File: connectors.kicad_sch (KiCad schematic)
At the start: 2 parts, among them J1 CM4_Plug_Module_Hirose_DF40_2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

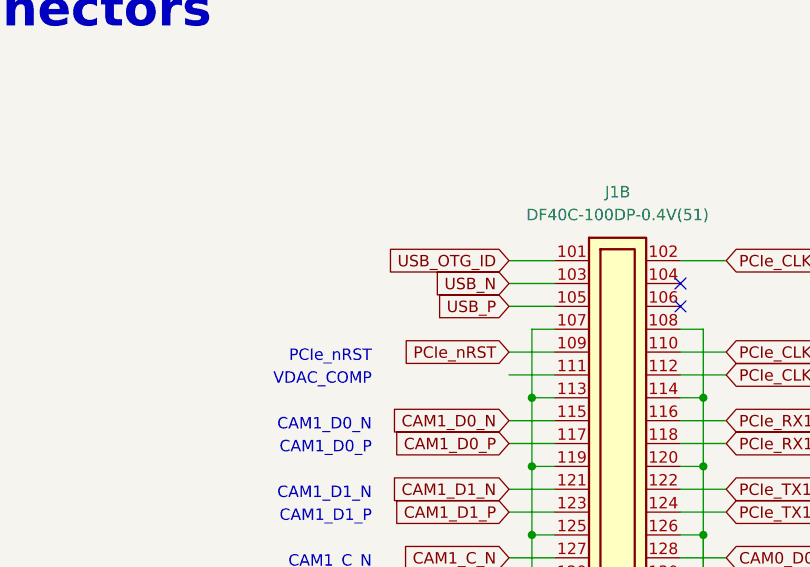
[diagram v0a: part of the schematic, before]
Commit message: [#54828] Add USB hub, change LBEE5PK2AE connection to USB
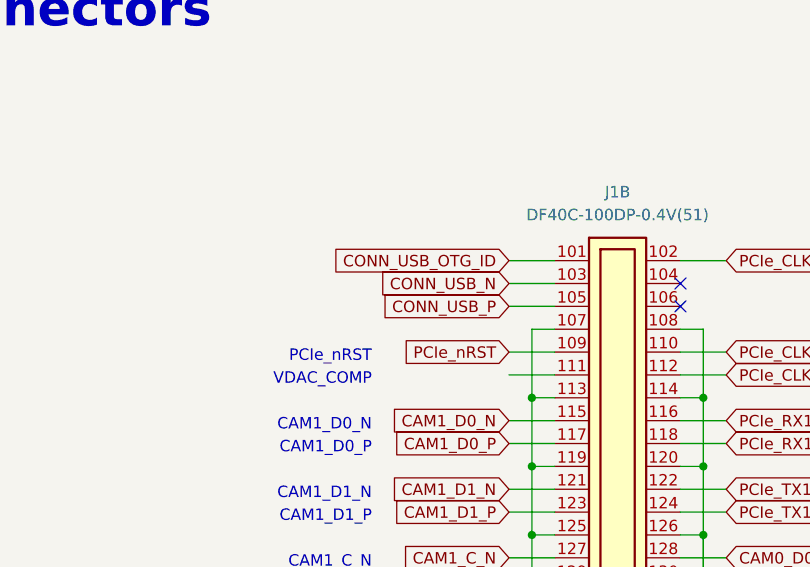
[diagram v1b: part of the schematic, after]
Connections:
- net USB_N renamed CONN_USB_N
- net USB_OTG_ID renamed CONN_USB_OTG_ID
- net USB_P renamed CONN_USB_P
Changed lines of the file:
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@@
+    )
+  )
+  (global_label "CONN_USB_OTG_ID" (shape input) (at 283.21 78.74 180) (fields_autoplaced)
+    (effects (font (size 1.27 1.27)) (justify right))
+    (property "Intersheetrefs" "${INTERSHEET_REFS}" (at 262.8076 78.74 0)
+      (effects (font (size 1.27 1.27)) (justify right) hide)
     )
   )
@@
     )
   )
-  (global_label "USB_N" (shape input) (at 283.21 81.28 180) (fields_autoplaced)
-    (effects (font (size 1.27 1.27)) (justify right))
-    (property "Intersheetrefs" "${INTERSHEET_REFS}" (at 274.6888 81.2006 0)
+  (global_label "CONN_USB_N" (shape input) (at 283.21 81.28 180) (fields_autoplaced)
+    (effects (font (size 1.27 1.27)) (justify right))
+    (property "Intersheetrefs" "${INTERSHEET_REFS}" (at 267.8876 81.28 0)
       (effects (font (size 1.27 1.27)) (justify right) hide)
     )
@@
     )
   )
-  (global_label "USB_P" (shape input) (at 283.21 83.82 180) (fields_autoplaced)
-    (effects (font (size 1.27 1.27)) (justify right))
-    (property "Intersheetrefs" "${INTERSHEET_REFS}" (at 274.7493 83.7406 0)
+  (global_label "CONN_USB_P" (shape input) (at 283.21 83.82 180) (fields_autoplaced)
+    (effects (font (size 1.27 1.27)) (justify right))
+    (property "Intersheetrefs" "${INTERSHEET_REFS}" (at 267.9481 83.82 0)
       (effects (font (size 1.27 1.27)) (justify right) hide)
     )
@@
       (effects (font (size 1.27 1.27)) (justify right) hide)
     )
-  )
-  (global_label "USB_OTG_ID" (shape input) (at 283.21 78.74 180) (fields_autoplaced)
-    (effects (font (size 1.27 1.27)) (justify right))
-    (property "Intersheetrefs" "${INTERSHEET_REFS}" (at 269.6088 78.6606 0)
-      (effects (font (size 1.27 1.27)) (justify right) hide)
-    )

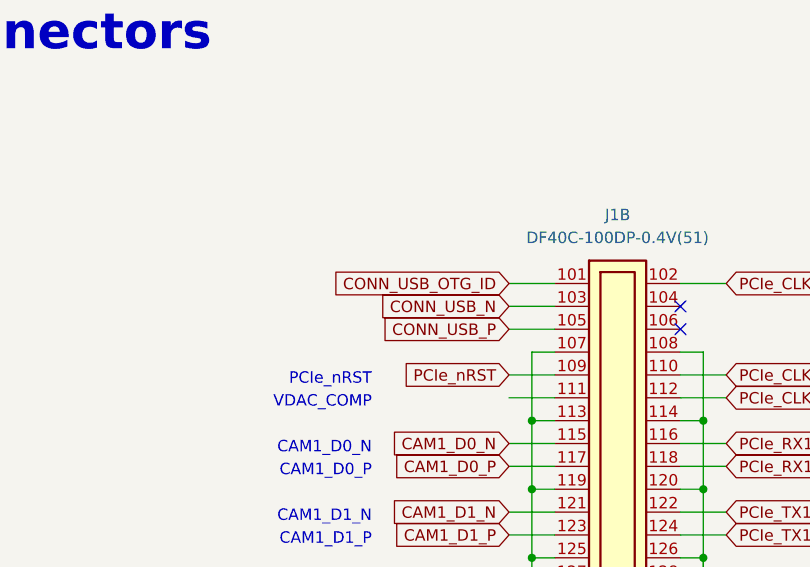
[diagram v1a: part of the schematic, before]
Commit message: [#54828] Add connections and external components to USB hub
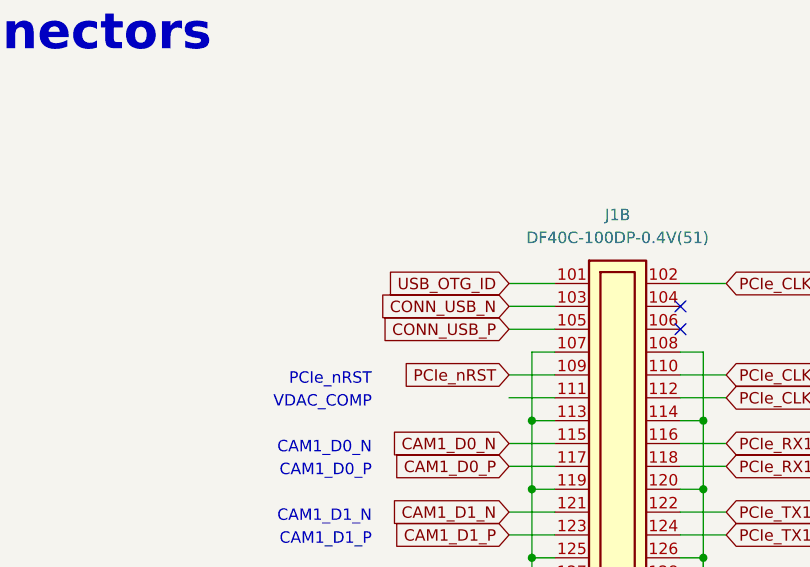
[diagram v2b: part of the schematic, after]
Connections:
- net CONN_USB_OTG_ID renamed USB_OTG_ID
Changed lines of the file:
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@@
-    )
-  )
-  (global_label "CONN_USB_OTG_ID" (shape input) (at 283.21 78.74 180) (fields_autoplaced)
-    (effects (font (size 1.27 1.27)) (justify right))
-    (property "Intersheetrefs" "${INTERSHEET_REFS}" (at 262.8076 78.74 0)
-      (effects (font (size 1.27 1.27)) (justify right) hide)
     )
   )
@@
       (effects (font (size 1.27 1.27)) (justify right) hide)
     )
+  )
+  (global_label "USB_OTG_ID" (shape input) (at 283.21 78.74 180) (fields_autoplaced)
+    (effects (font (size 1.27 1.27)) (justify right))
+    (property "Intersheetrefs" "${INTERSHEET_REFS}" (at 269.0367 78.74 0)
+      (effects (font (size 1.27 1.27)) (justify right) hide)
+    )

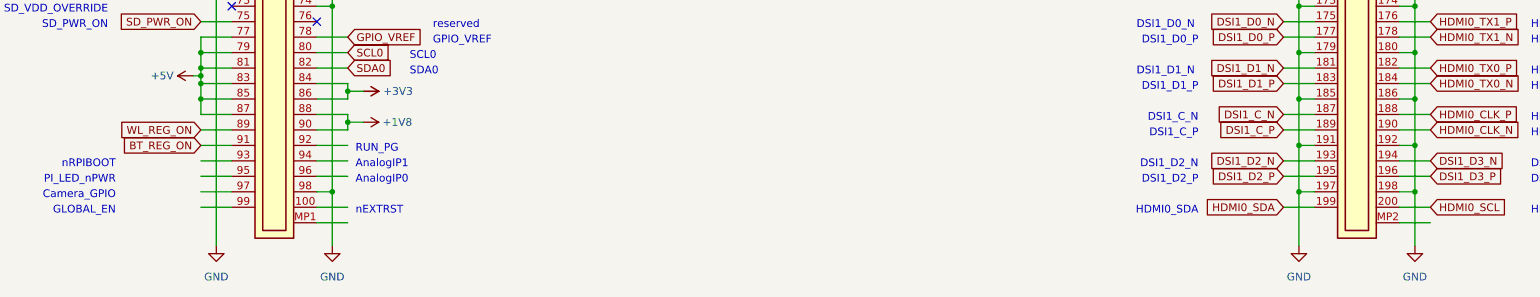
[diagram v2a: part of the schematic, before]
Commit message: [#54899] Simplify power sequencing, add missing connections
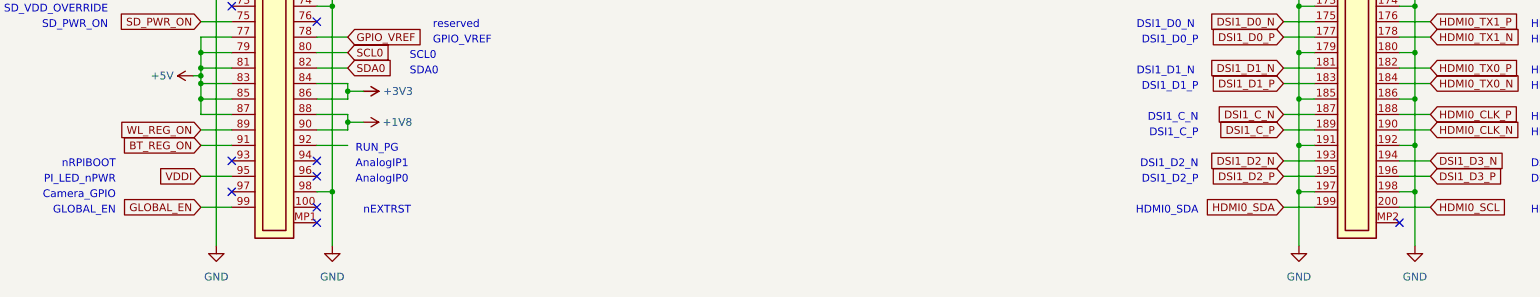
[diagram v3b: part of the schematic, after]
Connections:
- net VDDI: now reaches J1.95
- net GLOBAL_EN: now reaches J1.99
- no-connect marks 6 -> 13
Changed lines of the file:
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@@
   (no_connect (at 302.26 83.82))
   (no_connect (at 110.49 170.18))
+  (no_connect (at 124.46 205.74))
+  (no_connect (at 124.46 195.58))
+  (no_connect (at 110.49 200.66))
   (no_connect (at 105.41 104.14))
+  (no_connect (at 124.46 203.2))
   (no_connect (at 124.46 172.72))
+  (no_connect (at 302.26 205.74))
+  (no_connect (at 124.46 198.12))
+  (no_connect (at 110.49 195.58))
   (no_connect (at 129.54 101.6))
   (no_connect (at 302.26 81.28))
@@
     (stroke (width 0) (type default))
   )
-  (wire (pts (xy 124.46 195.58) (xy 129.54 195.58))
-    (stroke (width 0) (type default))
-  )
   (wire (pts (xy 302.26 106.68) (xy 307.34 106.68))
     (stroke (width 0) (type default))
@@
     (stroke (width 0) (type default))
   )
-  (wire (pts (xy 124.46 198.12) (xy 129.54 198.12))
-    (stroke (width 0) (type default))
-  )
   (wire (pts (xy 302.26 198.12) (xy 307.34 198.12))
     (stroke (width 0) (type default))
@@
     (stroke (width 0) (type default))
   )
-  (wire (pts (xy 302.26 205.74) (xy 307.34 205.74))
-    (stroke (width 0) (type default))
-  )
   (wire (pts (xy 285.75 86.36) (xy 285.75 93.98))
     (stroke (width 0) (type default))
@@
     (stroke (width 0) (type default))
   )
-  (wire (pts (xy 124.46 203.2) (xy 129.54 203.2))
-    (stroke (width 0) (type default))
-  )
   (wire (pts (xy 302.26 195.58) (xy 307.34 195.58))
     (stroke (width 0) (type default))
@@
     (stroke (width 0) (type default))
   )
-  (wire (pts (xy 124.46 205.74) (xy 129.54 205.74))
-    (stroke (width 0) (type default))
-  )
   (wire (pts (xy 283.21 190.5) (xy 288.29 190.5))
     (stroke (width 0) (type default))
@@
     (stroke (width 0) (type default))
   )
-  (wire (pts (xy 105.41 195.58) (xy 110.49 195.58))
-    (stroke (width 0) (type default))
-  )
   (wire (pts (xy 124.46 129.54) (xy 127 129.54))
     (stroke (width 0) (type default))
@@
     (stroke (width 0) (type default))
   )
-  (wire (pts (xy 105.41 200.66) (xy 110.49 200.66))
-    (stroke (width 0) (type default))
-  )
   (wire (pts (xy 285.75 109.22) (xy 288.29 109.22))
     (stroke (width 0) (type default))
@@
     (effects (font (size 1.27 1.27)) (justify left bottom))
   )
-  (text "nEXTRST" (at 130.81 204.47 0)
+  (text "nEXTRST" (at 132.08 204.47 0)
     (effects (font (size 1.27 1.27)) (justify left bottom))
   )
@@
     )
   )
+  (global_label "VDDI" (shape input) (at 105.41 198.12 180) (fields_autoplaced)
+    (effects (font (size 1.27 1.27)) (justify right))
+    (property "Intersheetrefs" "${INTERSHEET_REFS}" (at 98.1914 198.12 0)
+      (effects (font (size 1.27 1.27)) (justify right) hide)
+    )
+  )
   (global_label "SD_PWR_ON" (shape input) (at 105.41 172.72 180) (fields_autoplaced)
     (effects (font (size 1.27 1.27)) (justify right))
@@
       (effects (font (size 1.27 1.27)) (justify right) hide)
     )
+  )
+  (global_label "GLOBAL_EN" (shape input) (at 105.41 203.2 180) (fields_autoplaced)
+    (effects (font (size 1.27 1.27)) (justify right))
+    (property "Intersheetrefs" "${INTERSHEET_REFS}" (at 91.9624 203.2 0)
+      (effects (font (size 1.27 1.27)) (justify right) hide)
+    )

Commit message: [#54899] Re-annotate components
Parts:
- renumbered R74 to R1
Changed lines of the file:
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@@
   (symbol (lib_id "antmicropower:+5V") (at 104.14 181.61 90) (unit 1)
     (in_bom yes) (on_board yes) (dnp no)
-    (property "Reference" "#PWR0110" (at 106.68 166.37 0)
+    (property "Reference" "#PWR02" (at 106.68 166.37 0)
       (effects (font (size 1.27 1.27) (thickness 0.15)) (justify left bottom) hide)
     )
@@
       (project "polarfire-som"
         (path "/db4a0d3e-2eb3-499e-977d-6eb378cfd3ed/1a89b4c6-5d95-4c13-8da9-62b42c0a8ed9"
-          (reference "#PWR0110") (unit 1)
+          (reference "#PWR02") (unit 1)
         )
       )
@@
   (symbol (lib_id "antmicropower:+3V3") (at 132.08 184.15 270) (unit 1)
     (in_bom yes) (on_board yes) (dnp no)
-    (property "Reference" "#PWR0104" (at 129.54 199.39 0)
+    (property "Reference" "#PWR05" (at 129.54 199.39 0)
       (effects (font (size 1.27 1.27) (thickness 0.15)) (justify left bottom) hide)
     )
@@
       (project "polarfire-som"
         (path "/db4a0d3e-2eb3-499e-977d-6eb378cfd3ed/1a89b4c6-5d95-4c13-8da9-62b42c0a8ed9"
-          (reference "#PWR0104") (unit 1)
+          (reference "#PWR05") (unit 1)
         )
       )
@@
   (symbol (lib_id "antmicropower:+5V") (at 281.94 135.89 90) (unit 1)
     (in_bom yes) (on_board yes) (dnp no)
-    (property "Reference" "#PWR0101" (at 284.48 120.65 0)
+    (property "Reference" "#PWR07" (at 284.48 120.65 0)
       (effects (font (size 1.27 1.27) (thickness 0.15)) (justify left bottom) hide)
     )
@@
       (project "polarfire-som"
         (path "/db4a0d3e-2eb3-499e-977d-6eb378cfd3ed/1a89b4c6-5d95-4c13-8da9-62b42c0a8ed9"
-          (reference "#PWR0101") (unit 1)
+          (reference "#PWR07") (unit 1)
         )
       )
@@
   (symbol (lib_id "antmicropower:GND") (at 107.95 209.55 0) (unit 1)
     (in_bom yes) (on_board yes) (dnp no) (fields_autoplaced)
-    (property "Reference" "#PWR0106" (at 116.84 212.09 0)
+    (property "Reference" "#PWR03" (at 116.84 212.09 0)
       (effects (font (size 1.27 1.27) (thickness 0.15)) (justify left bottom) hide)
     )
@@
       (project "polarfire-som"
         (path "/db4a0d3e-2eb3-499e-977d-6eb378cfd3ed/1a89b4c6-5d95-4c13-8da9-62b42c0a8ed9"
-          (reference "#PWR0106") (unit 1)
+          (reference "#PWR03") (unit 1)
         )
       )
@@
   (symbol (lib_id "antmicropower:GND") (at 285.75 209.55 0) (unit 1)
     (in_bom yes) (on_board yes) (dnp no) (fields_autoplaced)
-    (property "Reference" "#PWR0102" (at 294.64 212.09 0)
+    (property "Reference" "#PWR08" (at 294.64 212.09 0)
       (effects (font (size 1.27 1.27) (thickness 0.15)) (justify left bottom) hide)
     )
@@
       (project "polarfire-som"
         (path "/db4a0d3e-2eb3-499e-977d-6eb378cfd3ed/1a89b4c6-5d95-4c13-8da9-62b42c0a8ed9"
-          (reference "#PWR0102") (unit 1)
+          (reference "#PWR08") (unit 1)
         )
       )
@@
   (symbol (lib_id "antmicropower:GND") (at 304.8 209.55 0) (unit 1)
     (in_bom yes) (on_board yes) (dnp no) (fields_autoplaced)
-    (property "Reference" "#PWR0103" (at 313.69 212.09 0)
+    (property "Reference" "#PWR09" (at 313.69 212.09 0)
       (effects (font (size 1.27 1.27) (thickness 0.15)) (justify left bottom) hide)
     )
@@
       (project "polarfire-som"
         (path "/db4a0d3e-2eb3-499e-977d-6eb378cfd3ed/1a89b4c6-5d95-4c13-8da9-62b42c0a8ed9"
-          (reference "#PWR0103") (unit 1)
+          (reference "#PWR09") (unit 1)
         )
       )
@@
   (symbol (lib_id "antmicropower:GND") (at 127 209.55 0) (unit 1)
     (in_bom yes) (on_board yes) (dnp no) (fields_autoplaced)
-    (property "Reference" "#PWR0109" (at 135.89 212.09 0)
+    (property "Reference" "#PWR04" (at 135.89 212.09 0)
       (effects (font (size 1.27 1.27) (thickness 0.15)) (justify left bottom) hide)
     )
@@
       (project "polarfire-som"
         (path "/db4a0d3e-2eb3-499e-977d-6eb378cfd3ed/1a89b4c6-5d95-4c13-8da9-62b42c0a8ed9"
-          (reference "#PWR0109") (unit 1)
+          (reference "#PWR04") (unit 1)
         )
       )
@@
   (symbol (lib_id "antmicropower:+1V8") (at 132.08 189.23 270) (unit 1)
     (in_bom yes) (on_board yes) (dnp no)
-    (property "Reference" "#PWR0105" (at 129.54 204.47 0)
+    (property "Reference" "#PWR06" (at 129.54 204.47 0)
       (effects (font (size 1.27 1.27) (thickness 0.15)) (justify left bottom) hide)
     )
@@
       (project "polarfire-som"
         (path "/db4a0d3e-2eb3-499e-977d-6eb378cfd3ed/1a89b4c6-5d95-4c13-8da9-62b42c0a8ed9"
-          (reference "#PWR0105") (unit 1)
+          (reference "#PWR06") (unit 1)
         )
       )
@@
   (symbol (lib_id "antmicroResistors0402:R_100k_0402") (at 90.17 132.08 0) (unit 1)
     (in_bom yes) (on_board yes) (dnp no)
-    (property "Reference" "R74" (at 90.17 130.81 0)
+    (property "Reference" "R1" (at 90.17 130.81 0)
       (effects (font (size 1.27 1.27) (thickness 0.15)) (justify right))
     )
@@
       (project "polarfire-som"
         (path "/db4a0d3e-2eb3-499e-977d-6eb378cfd3ed/1a89b4c6-5d95-4c13-8da9-62b42c0a8ed9"
-          (reference "R74") (unit 1)
+          (reference "R1") (unit 1)
         )
       )
@@
   (symbol (lib_id "antmicropower:+3V3") (at 86.36 132.08 90) (unit 1)
     (in_bom yes) (on_board yes) (dnp no)
-    (property "Reference" "#PWR0244" (at 88.9 116.84 0)
+    (property "Reference" "#PWR01" (at 88.9 116.84 0)
       (effects (font (size 1.27 1.27) (thickness 0.15)) (justify left bottom) hide)
     )
@@
       (project "polarfire-som"
         (path "/db4a0d3e-2eb3-499e-977d-6eb378cfd3ed/1a89b4c6-5d95-4c13-8da9-62b42c0a8ed9"
-          (reference "#PWR0244") (unit 1)
-        )
-      )
+          (reference "#PWR01") (unit 1)
+        )
+      )
